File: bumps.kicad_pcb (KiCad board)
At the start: 2 copper layers, 111.1 x 65.4 mm, 135 parts, among them M1 CONN_1, M2 CONN_1, M3 CONN_1, P1 DIL6, P10 Mot-A, P11 Mot-A, P12 Mot-X, P13 T1, P14 T2, P15 T3, P16 MPower, P17 PWM-2, P18 PWM-1, P19 END-X, P2 DIL6, P20 END-Y, P21 END-Z, P22 Mot-X, P23 Mot-Y, P24 Mot-Y, P25 Mot-Z, P26 Mot-Z, P27 Aux, P28 KillSwitch, P29 PWM, P3 Mot-E, P30 CONN_01X01, P31 CONN_01X01, P4 Mot-E, P5 DIL6, P6 DIL6, P7 DIL6, P8 P8 Header, P9 P9 Header, Q1 IRLB8743PBF, Q2 IRLB8743PBF, Q3 FDS9926A, Q4 FDS9926A, U1 Motor-2, U2 Motor-4, U3 Motor-5, U4 Motor-3, U5 Motor-1, U6 MC34063, U7 AP1117/3.3, U8 PC817

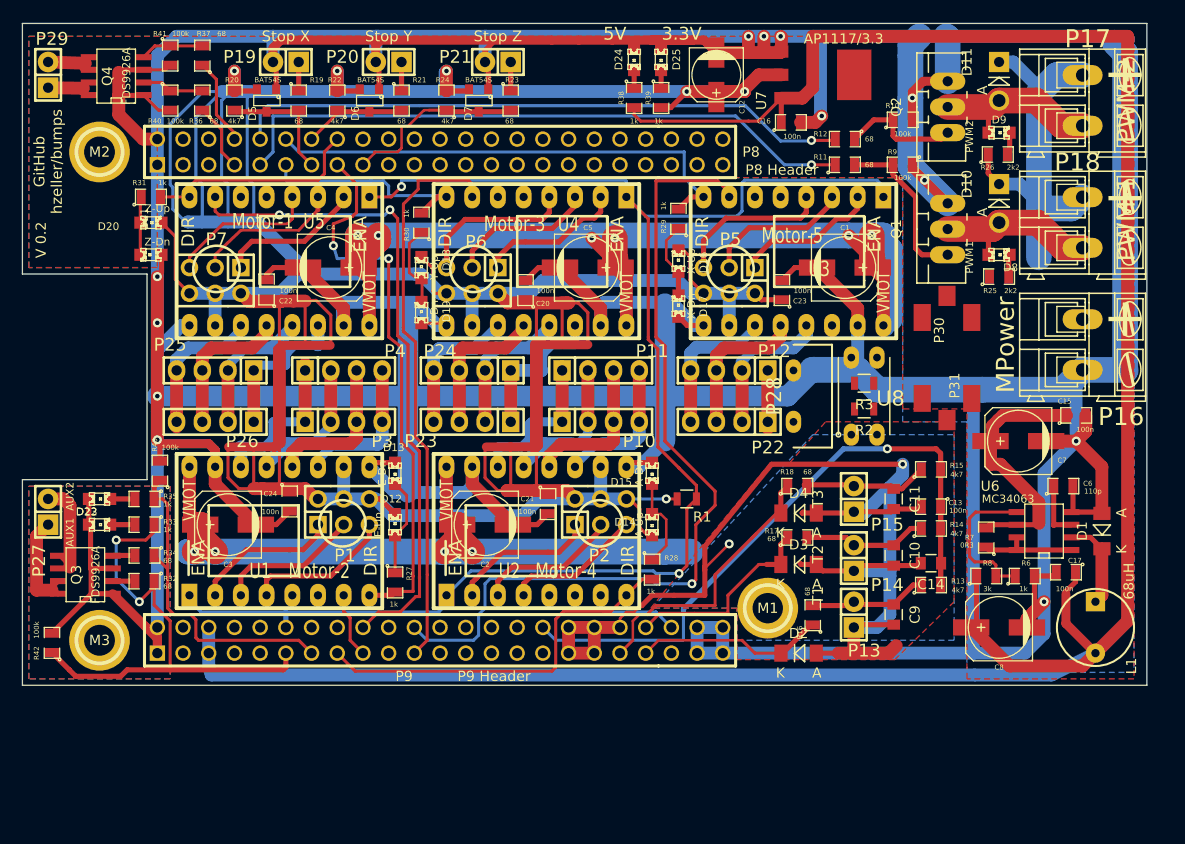
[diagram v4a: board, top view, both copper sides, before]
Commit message: o Use some current standard components.
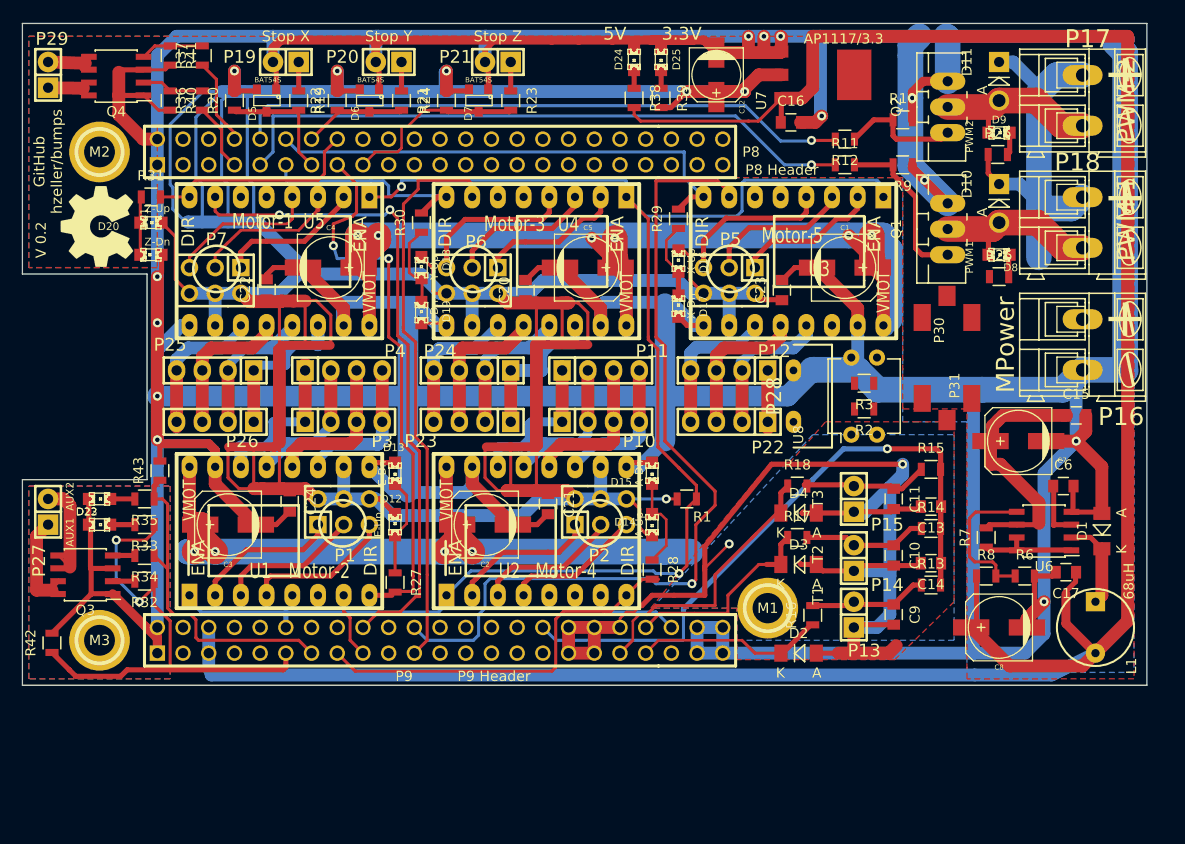
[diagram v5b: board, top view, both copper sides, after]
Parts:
- added G***: LOGO, bumps:OSH-LOGO, F.Cu at (55.0, 48.0)
- C13, C15, C16, C17, C20, C21, C22, C23, C24, C6: footprint SMD_Packages:SM0805 -> Capacitors_SMD:C_0805
- Q3, Q4, U6: footprint SOIC_Packages:SOIC-8_N -> Housings_SOIC:SOIC-8_3.9x4.9mm_Pitch1.27mm
- R10, R11, R12, R13, R14, R15, R16, R17, R18, R19, R20, R21, R22, R23, R24, R25, R26, R27, R28, R29, R30, R31, R32, R33, R34, R35, R36, R37, R38, R39, R40, R41, R42, R43, R6, R7, R8, R9: footprint SMD_Packages:SM0805 -> Resistors_SMD:R_0805
- U8: footprint bumps:DIL-4 -> Housings_DIP:DIP-4_W7.62mm
- moved U8 4.02 mm to (129.5, 68.6), turned to 90 degrees
- turned Q3 to 180 degrees
- turned Q4 to 180 degrees
- turned U6 to 180 degrees
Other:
- board text removed: "AUX OC"
- board text removed: "End-X"
- board text removed: "End-Y"
- board text removed: "End-Z"
- board text removed: "PWM OC"
- board text removed: "PWM-1"
- board text removed: "PWM-2"
- board text removed: "PWM3"
- board text removed: "PWM4"
- board text removed: "Power"
- board text removed: "TODO OSH logo"

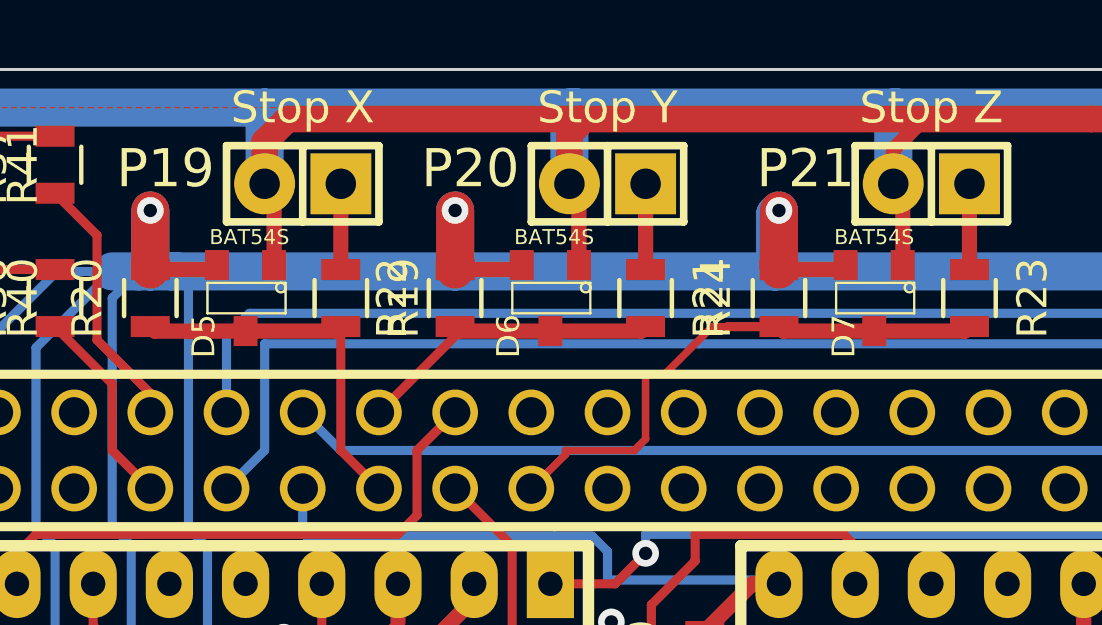
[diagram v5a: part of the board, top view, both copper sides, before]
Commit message: o More standard footprint conversions.
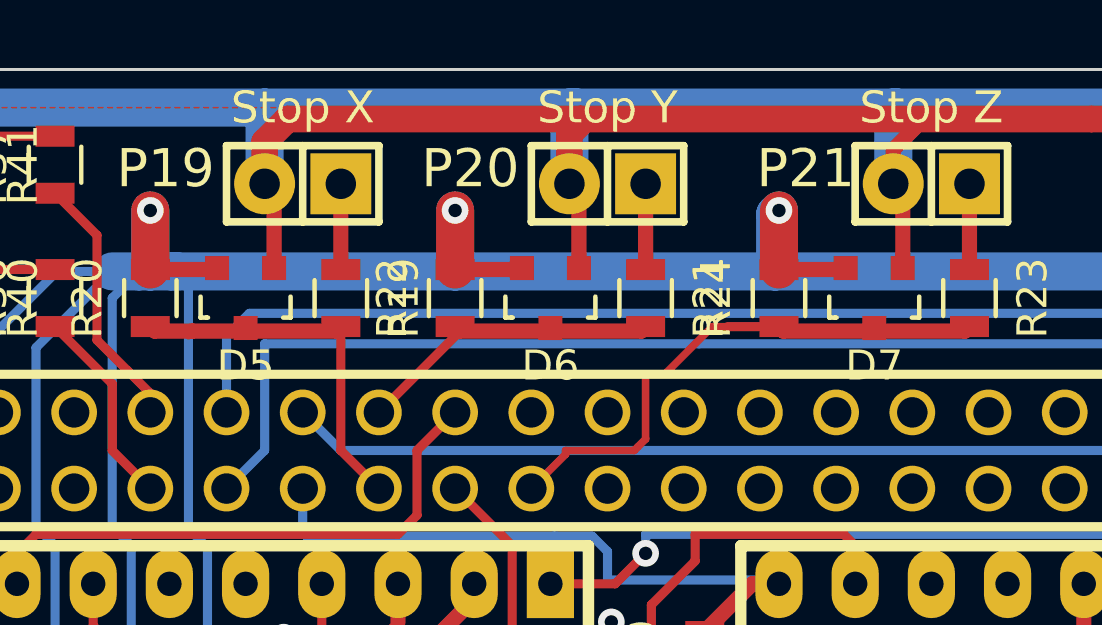
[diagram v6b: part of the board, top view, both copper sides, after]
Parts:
- D5, D6, D7: footprint SMD_Packages:SOT23 -> Housings_SOT-23_SOT-143_TSOT-6:SOT-23

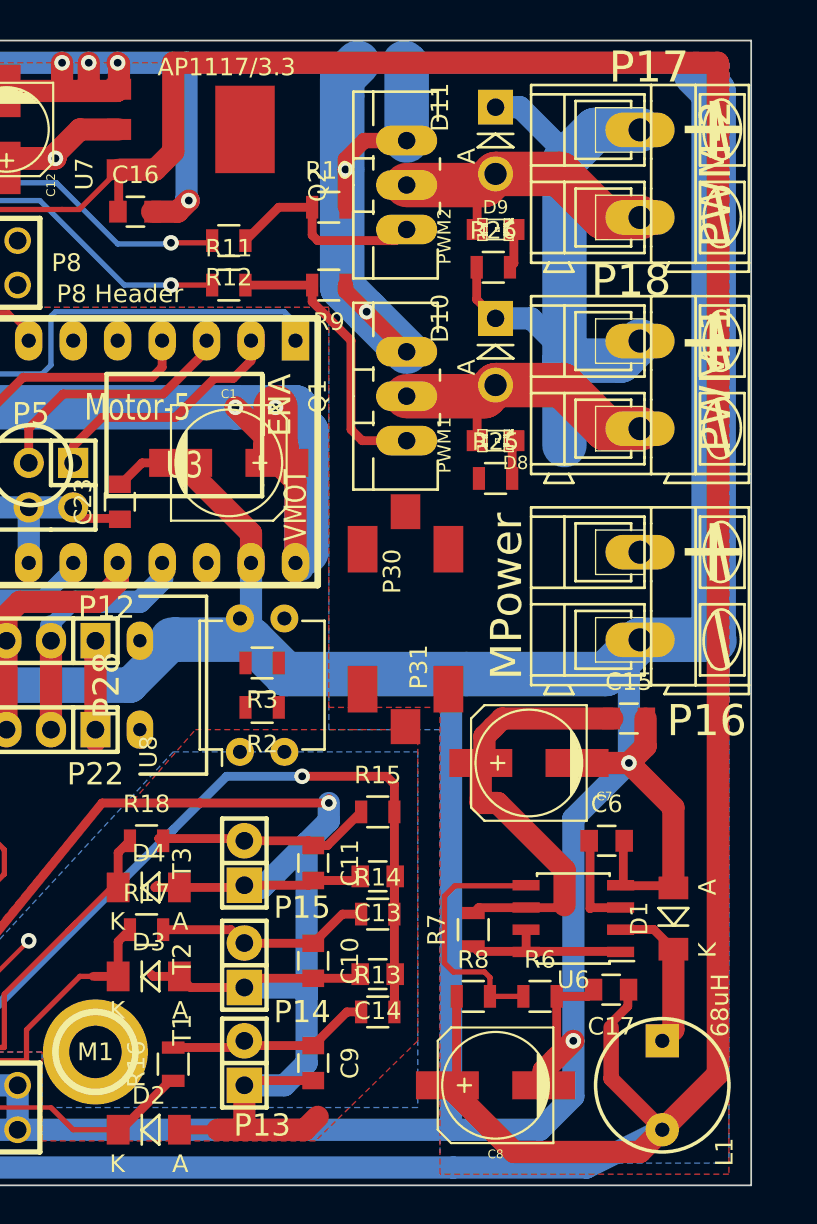
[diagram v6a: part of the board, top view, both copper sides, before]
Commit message: o Design for Manufacturing: choose the same kind of diode for the   switching power supply and the snubber diode to reduce different   component BOM count.
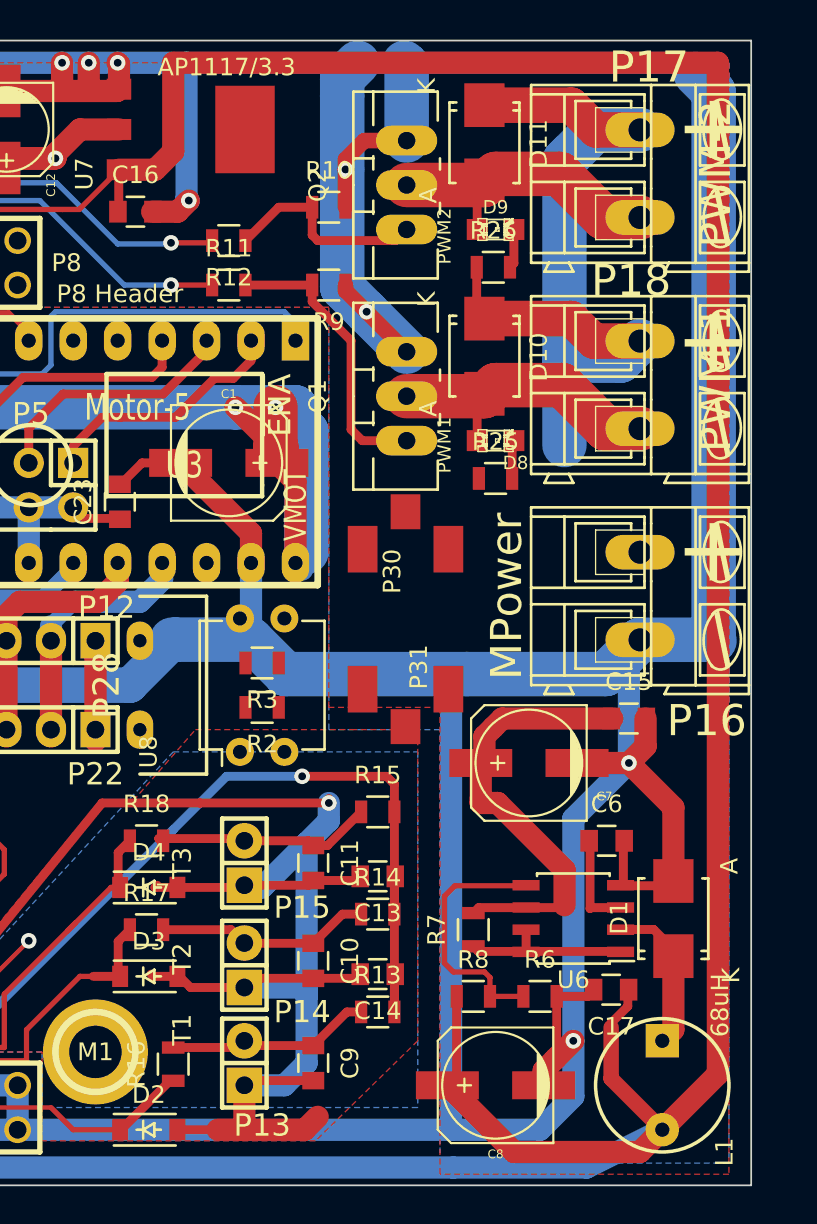
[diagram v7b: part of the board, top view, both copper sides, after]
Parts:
- D1: value Schottky -> STPS1H100; footprint Diodes_SMD:Diode-MiniMELF_Standard -> Diodes_SMD:Diode-SMB_Standard
- D10, D11: value SB180 -> STPS1H100; footprint Diodes_ThroughHole:Diode_DO-41_SOD81_Vertical_AnodeUp -> Diodes_SMD:Diode-SMB_Standard
- D2, D3, D4: footprint Diodes_SMD:Diode-MiniMELF_Standard -> Diodes_SMD:SOD-123
- moved D10 2.25 mm to (143.5, 46.0)
- moved D11 2.13 mm to (143.5, 33.8)
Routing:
- net VMOT: track 247.3 -> 255.4 mm

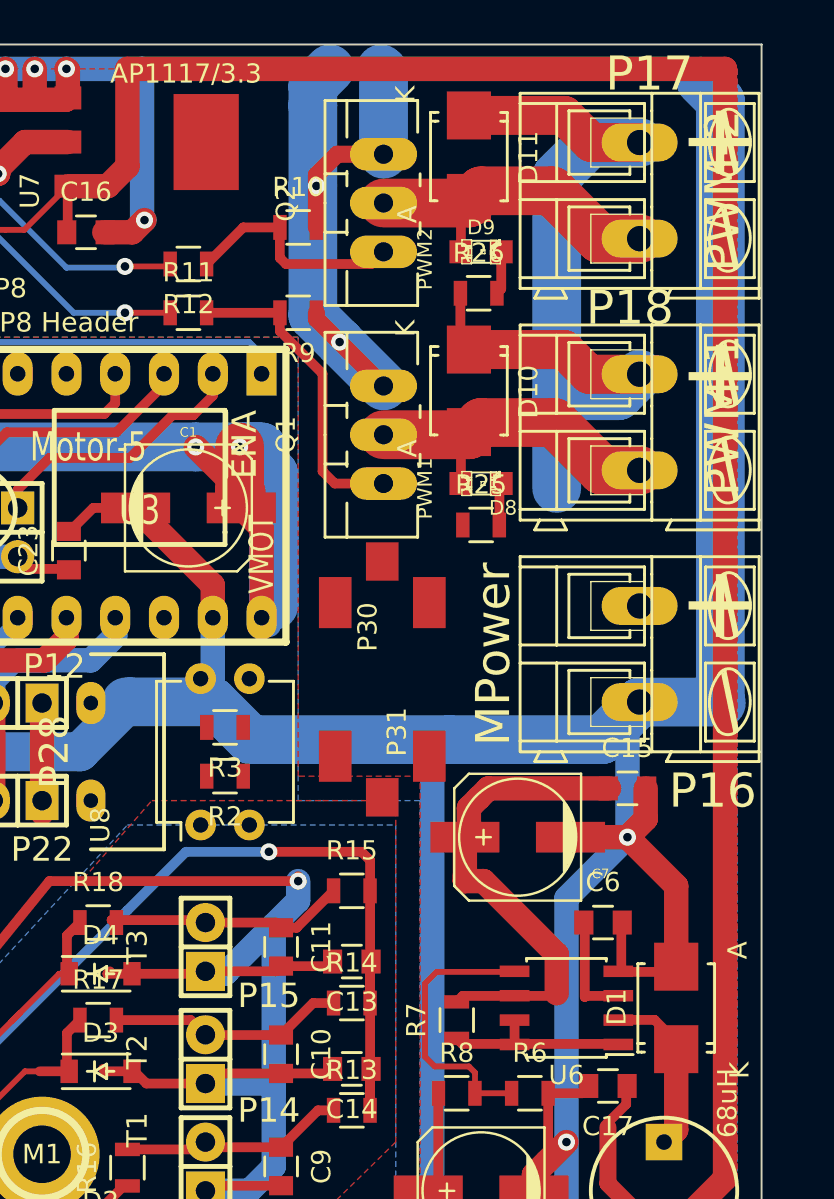
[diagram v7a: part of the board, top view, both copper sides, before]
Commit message: o Use BUK9Y43 as power PWM transistor. SMD is easier to solder.
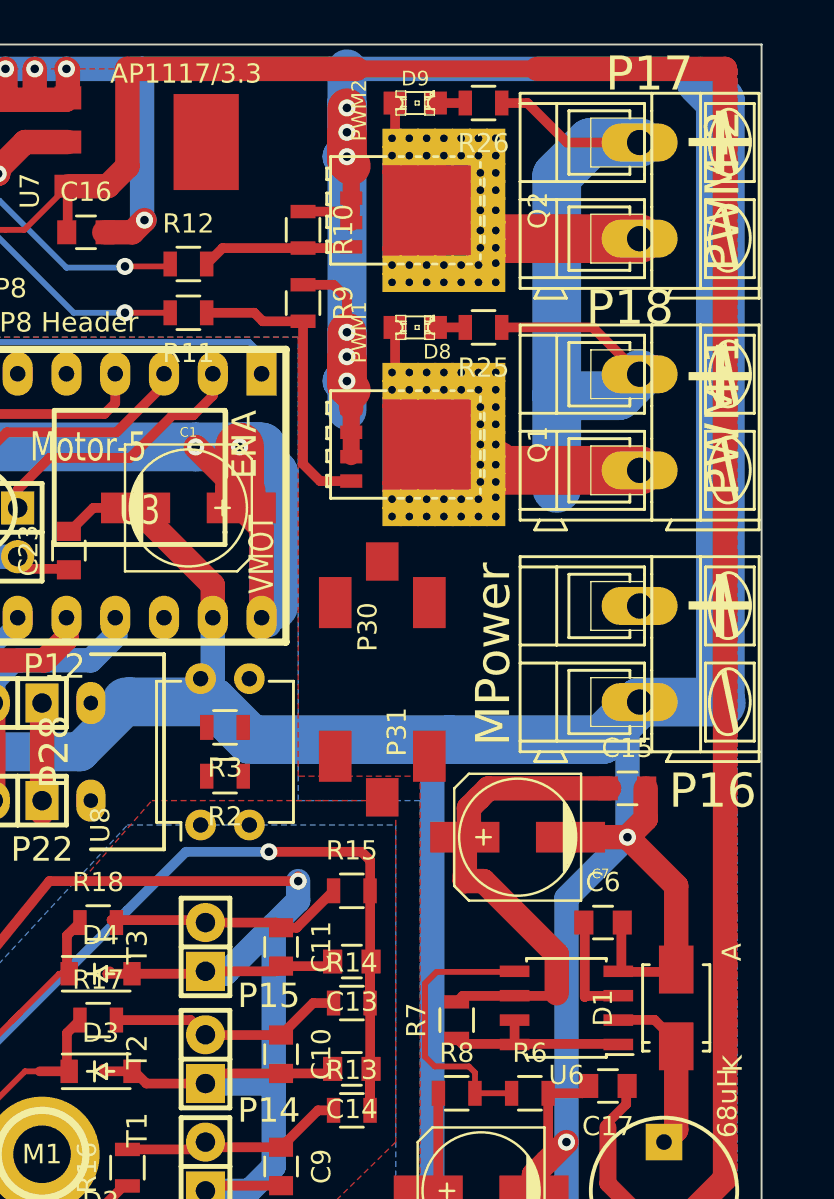
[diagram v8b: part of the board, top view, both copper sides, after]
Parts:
- removed D10, D11: STPS1H100, Diodes_SMD:Diode-SMB_Standard
- D1: value STPS1H100 -> STPS130A; footprint Diodes_SMD:Diode-SMB_Standard -> Diodes_SMD:Diode-SMA_Standard
- Q1, Q2: value IRLB8743PBF -> BUK9Y43; footprint Transistors_TO-220:TO-220_Neutral123_Vertical_LargePads -> Power_Packages_SMD:SOT-669_LFPAK_ThermalVias-1
- moved R25 10.3 mm to (144.3, 42.7), turned to 180 degrees
- moved R26 9.91 mm to (144.3, 31.0), turned to 180 degrees
- moved D8 8.82 mm to (140.7, 42.7)
- moved D9 8.47 mm to (140.7, 31.0)
- moved Q1 1.25 mm to (140.2, 48.8), turned to 270 degrees
- moved Q2 1.20 mm to (140.2, 36.6), turned to 270 degrees
- moved R9 0.57 mm to (134.9, 41.4), turned to 270 degrees
- moved R10 0.28 mm to (134.9, 37.6), turned to 270 degrees
- turned R11 to 180 degrees
- turned R12 to 0 degrees
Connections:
- D8 pad 1: Net-(D10-Pad2) -> Net-(D8-Pad1)
- D9 pad 1: Net-(D11-Pad2) -> Net-(D9-Pad1)
- P17 pad 2: Net-(D11-Pad2) -> Net-(D9-Pad1)
- P18 pad 2: Net-(D10-Pad2) -> Net-(D8-Pad1)
- Q1 pad 1: Net-(Q1-Pad1) -> GND
- Q1 pad 2: Net-(D10-Pad2) -> GND
- Q2 pad 1: Net-(Q2-Pad1) -> GND
- Q2 pad 2: Net-(D11-Pad2) -> GND
- R10 pad 1: Net-(Q2-Pad1) -> GND
- R10 pad 2: GND -> Net-(Q2-Pad4)
- R11 pad 1: PWM_1 -> Net-(Q1-Pad4)
- R11 pad 2: Net-(Q1-Pad1) -> PWM_1
- R12 pad 1: Net-(Q2-Pad1) -> PWM_2
- R12 pad 2: PWM_2 -> Net-(Q2-Pad4)
- R9 pad 2: Net-(Q1-Pad1) -> Net-(Q1-Pad4)
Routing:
- net Net-(D10-Pad2): track 18.2 -> 0.00 mm
- net Net-(D11-Pad2): track 18.2 -> 0.00 mm
- net Net-(D8-Pad1): track 0.00 -> 18.1 mm
- net Net-(Q1-Pad1): track 16.4 -> 0.00 mm
- net Net-(Q1-Pad4): track 0.00 -> 15.5 mm
- net Net-(D9-Pad1): track 0.00 -> 14.0 mm
- net Net-(Q2-Pad1): track 12.0 -> 0.00 mm
- net GND: track 822.6 -> 830.7 mm, vias 12 -> 16
- net Net-(Q2-Pad4): track 0.00 -> 7.90 mm
- net VMOT: track 255.4 -> 249.3 mm
- net Net-(D8-Pad2): track 2.52 -> 1.56 mm
- net Net-(D9-Pad2): track 2.25 -> 1.56 mm
